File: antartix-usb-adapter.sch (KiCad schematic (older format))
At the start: 113 parts, among them IC1 FT2232D, J1 QTE-020-04-L-D-A, J2 0022232041, J3 614004185023, J4 WE_629105150521, J5 614004185023, J6 614004185023, U1 PCT2075GVX, U2 PAC1934T-I_JQ, U3 USB2514B-I_M2, U4 TPS2024DR, U5 TPS2024DR, U6 TPS2024DR, Y1 7C-24.000MBB-T, Y2 MQ-6.000-12-30_30_

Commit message: Rename alt upstream lanes
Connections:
- net USB_D_CON_N renamed USB_ALT_UP_N
- net USB_D_CON_P renamed USB_ALT_UP_P
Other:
- note added: "Micro USB conn - alternative upstream option"
- note removed: "Micro USB connector"
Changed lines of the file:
@@
 Wire Notes Line
 	4025 525  4025 6650
-Text Notes 12900 3075 0    118  ~ 0
-Micro USB connector
+Text Notes 11650 3075 0    118  ~ 0
+Micro USB conn - alternative upstream option
 Wire Notes Line
 	11575 2850 16075 2850
@@
 $EndComp
 Text Label 575  2225 0    50   ~ 0
-USB_D_CON_N
+USB_ALT_UP_N
 Text Label 575  2125 0    50   ~ 0
-USB_D_CON_P
+USB_ALT_UP_P
 Wire Wire Line
 	1125 2125 550  2125
@@
 $EndComp
 Text Label 13625 3800 2    50   ~ 0
-USB_D_CON_N
+USB_ALT_UP_N
 Text Label 13625 3900 2    50   ~ 0
-USB_D_CON_P
+USB_ALT_UP_P
 Wire Wire Line
 	12625 3900 12900 3900

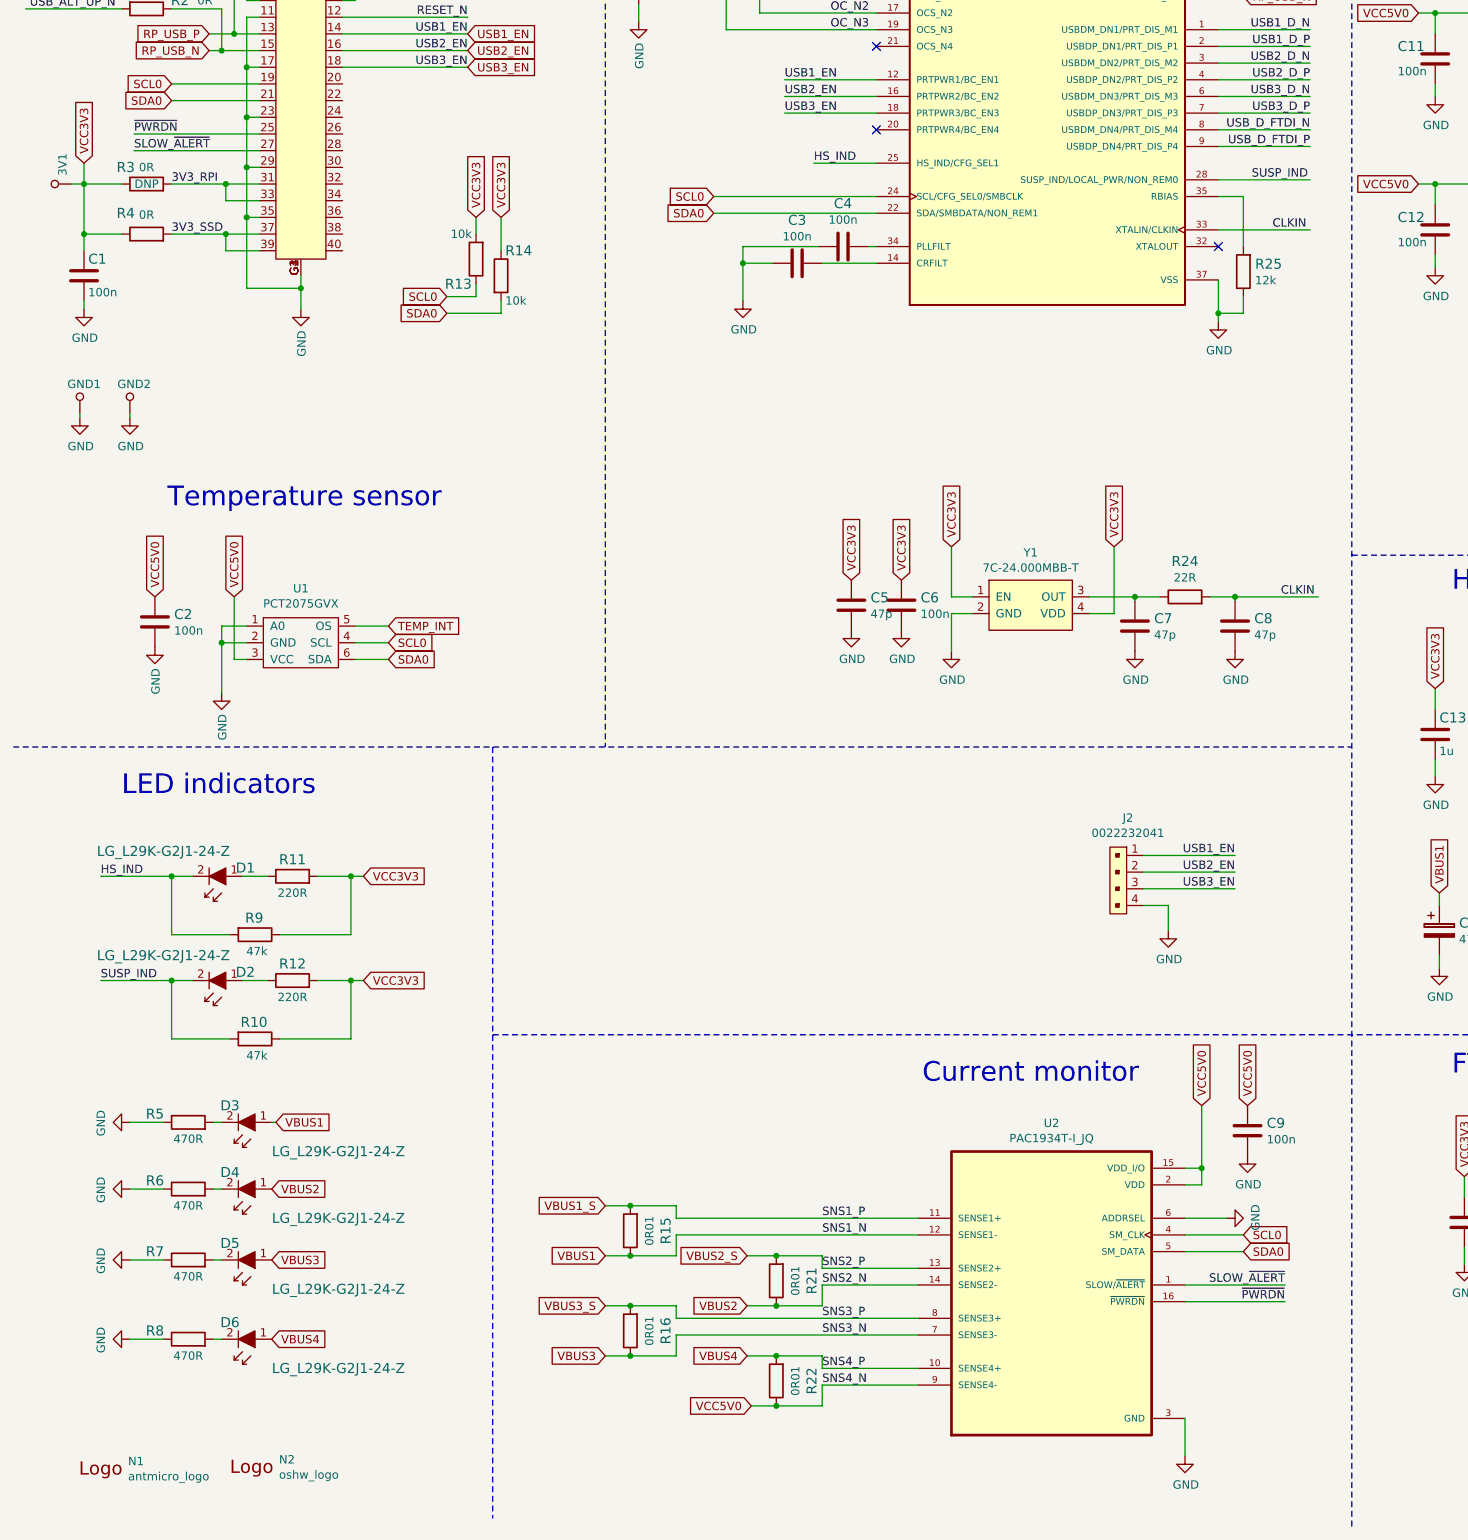
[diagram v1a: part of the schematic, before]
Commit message: Add FTDI and LEDs
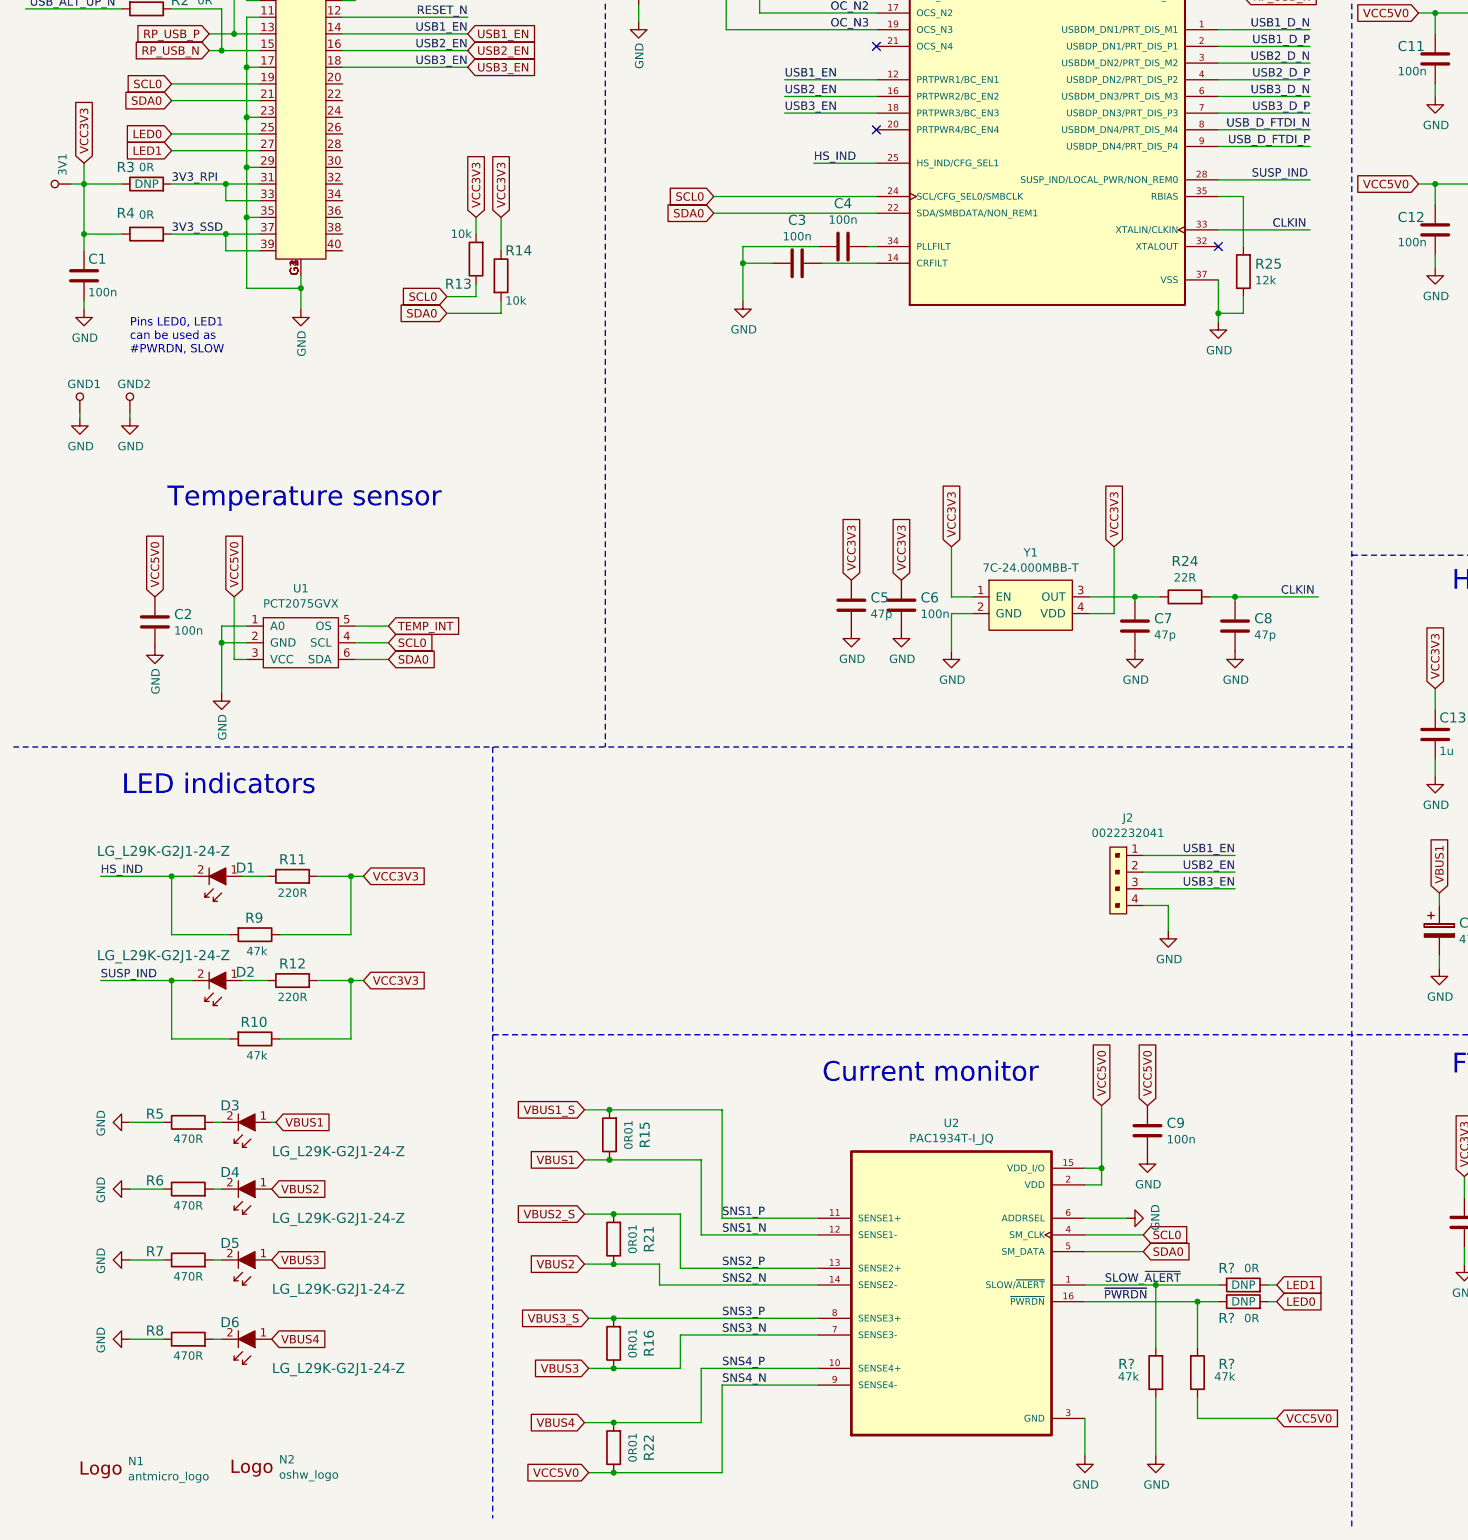
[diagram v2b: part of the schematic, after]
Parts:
- added R? (x2): R_47k_0402, antartix-arty-controller-footprints:0402-res, symbol antartix-arty-controller:R_47k_0402
- added R? (x2): R_0R_0805, antmicro-footprints:0805-res, symbol antmicroResistorsmisc:R_0R_0805
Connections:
- net GND: now also R?.1
- net SLOW_~ALERT: now also R?.1, R?.2; no longer J1.27
- net VCC5V0: now also R?.1
- net ~PWRDN: now also R?.1, R?.2; no longer J1.25
- new net LED0: J1.25, R?.2
- new net LED1: J1.27, R?.2
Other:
- note added: "Pins LED0, LED1\ncan be used as \n#PWRDN, SLOW"
- moved on the sheet: C9, R15, R16, R21, R22, U2

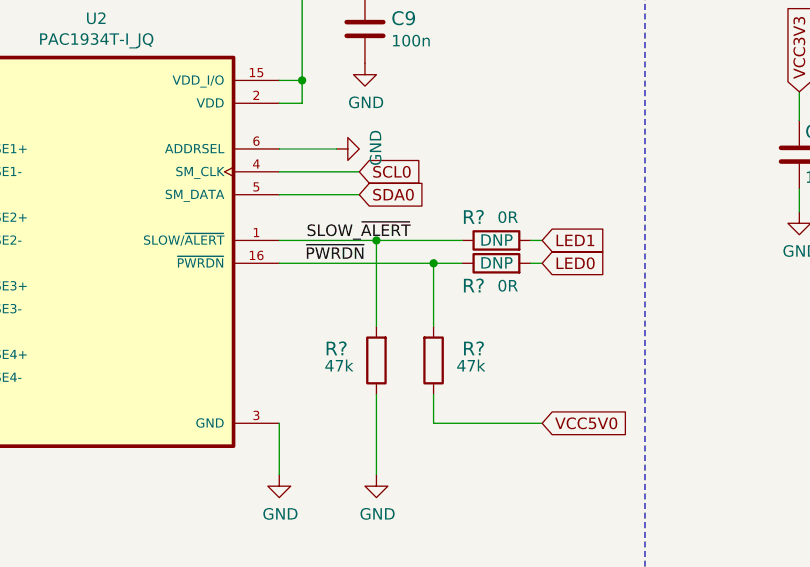
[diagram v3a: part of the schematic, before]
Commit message: Reduce board size, update connector placement
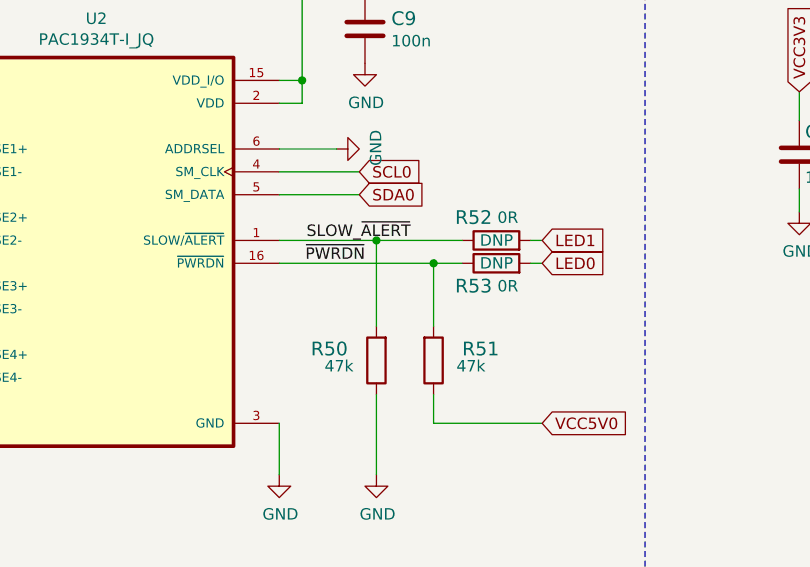
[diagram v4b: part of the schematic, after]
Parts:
- gave numbers to parts that had none: 4
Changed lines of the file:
@@
 P 7325 10400
 AR Path="/60F36AEC" Ref="R?"  Part="1"
-AR Path="/60924187/60F36AEC" Ref="R?"  Part="1"
-F 0 "R?" V 7375 10525 60  0000 L CNN
+AR Path="/60924187/60F36AEC" Ref="R50"  Part="1"
+F 0 "R50" V 7375 10525 60  0000 L CNN
 F 1 "R_47k_0402" H 7325 10250 60  0001 C CNN
 F 2 "antartix-arty-controller-footprints:0402-res" H 7525 10600 60  0001 L CNN
@@
 P 7850 9875
 AR Path="/60F3CD7D" Ref="R?"  Part="1"
-AR Path="/60924187/60F3CD7D" Ref="R?"  Part="1"
-F 0 "R?" H 7750 9975 60  0000 C CNN
+AR Path="/60924187/60F3CD7D" Ref="R52"  Part="1"
+F 0 "R52" H 7750 9975 60  0000 C CNN
 F 1 "R_0R_0805" H 7850 9725 60  0001 C CNN
 F 2 "antmicro-footprints:0805-res" H 8050 10075 60  0001 L CNN
@@
 P 7850 9975
 AR Path="/60F4C618" Ref="R?"  Part="1"
-AR Path="/60924187/60F4C618" Ref="R?"  Part="1"
-F 0 "R?" H 7750 9875 60  0000 C CNN
+AR Path="/60924187/60F4C618" Ref="R53"  Part="1"
+F 0 "R53" H 7750 9875 60  0000 C CNN
 F 1 "R_0R_0805" H 7850 9825 60  0001 C CNN
 F 2 "antmicro-footprints:0805-res" H 8050 10175 60  0001 L CNN
@@
 P 7575 10400
 AR Path="/610F9DE3" Ref="R?"  Part="1"
-AR Path="/60924187/610F9DE3" Ref="R?"  Part="1"
-F 0 "R?" V 7625 10525 60  0000 L CNN
+AR Path="/60924187/610F9DE3" Ref="R51"  Part="1"
+F 0 "R51" V 7625 10525 60  0000 L CNN
 F 1 "R_47k_0402" H 7575 10250 60  0001 C CNN
 F 2 "antartix-arty-controller-footprints:0402-res" H 7775 10600 60  0001 L CNN
@@
 P 7325 10900
 AR Path="/6113774D" Ref="#PWR?"  Part="1"
-AR Path="/60924187/6113774D" Ref="#PWR?"  Part="1"
-F 0 "#PWR?" H 7325 10650 50  0001 C CNN
+AR Path="/60924187/6113774D" Ref="#PWR0119"  Part="1"
+F 0 "#PWR0119" H 7325 10650 50  0001 C CNN
 F 1 "GND" H 7330 10727 50  0000 C CNN
 F 2 "" H 7325 10900 50  0001 C CNN

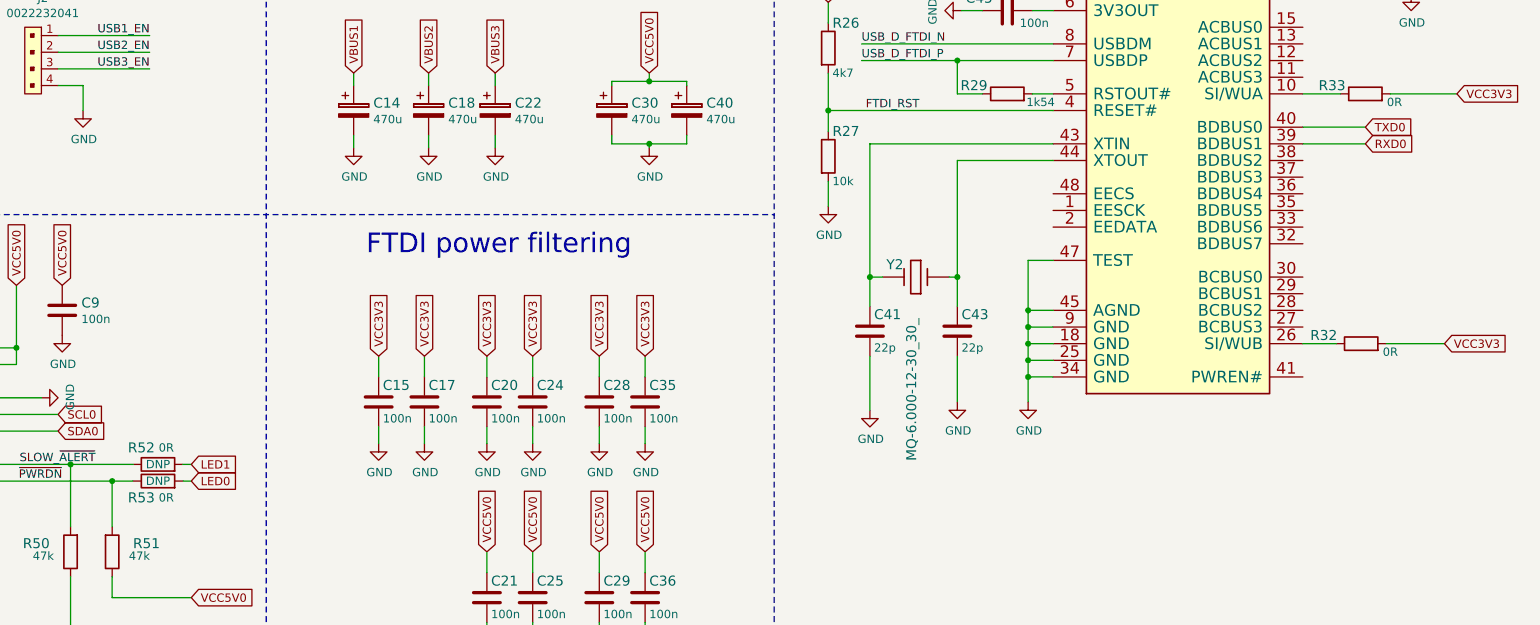
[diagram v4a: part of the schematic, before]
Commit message: Route buttons and HDMI
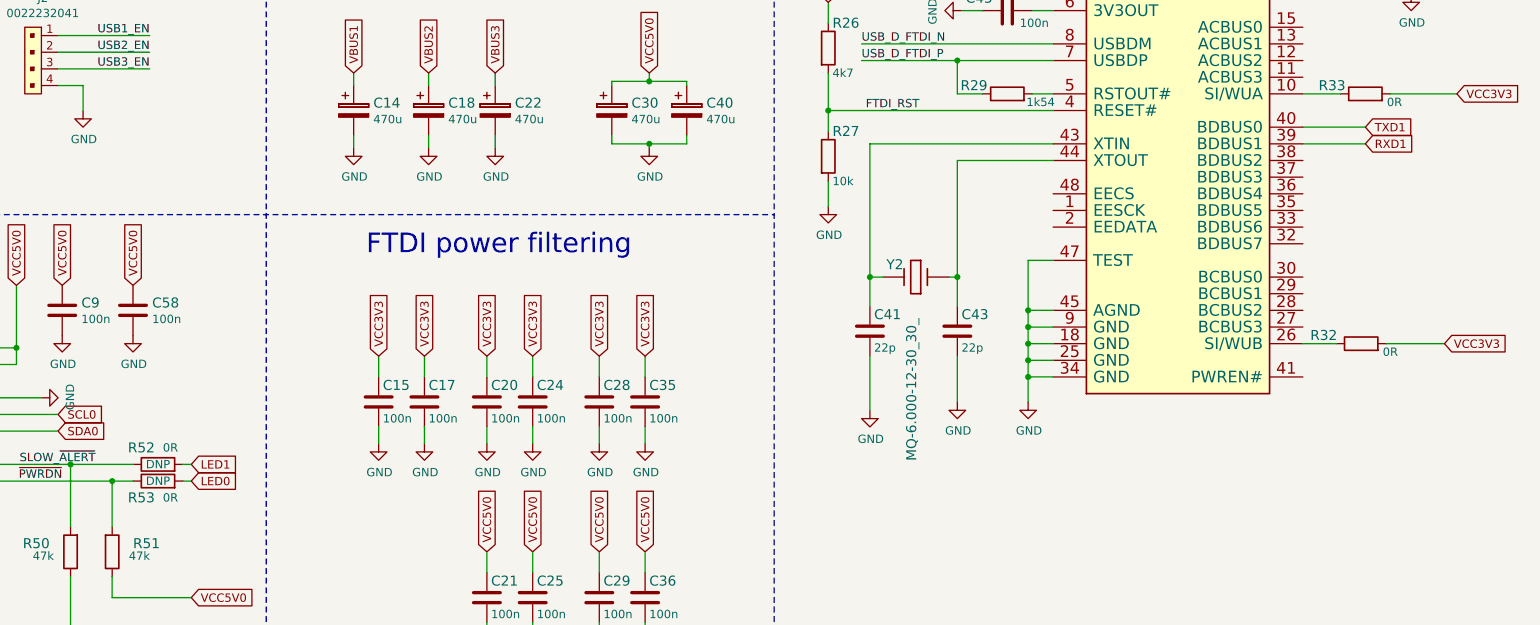
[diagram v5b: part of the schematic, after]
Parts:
- removed R52, R53: R_0R_0805, antmicro-footprints:0805-res, symbol antmicroResistorsmisc:R_0R_0805
- added C58: C_100n_0402, antartix-arty-controller-footprints:0402-cap, symbol antartix-arty-controller:C_100n_0402
- added R52, R53: R_0R_0402, antartix-arty-controller-footprints:0402-res, symbol antartix-arty-controller:R_0R_0402
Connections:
- net GND: now also C58.2
- net LED0: now also R53.2
- net LED1: now also R52.2
- net SLOW_~ALERT: now also R52.1
- net VCC5V0: now also C58.1
- net ~PWRDN: now also R53.1
- net RXD0 renamed RXD1
- net TXD0 renamed TXD1
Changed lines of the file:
@@
 $EndComp
 Text GLabel 15100 7850 2    50   Input ~ 0
-TXD0
+TXD1
 Text GLabel 15100 7950 2    50   Input ~ 0
-RXD0
+RXD1
 Wire Wire Line
 	15100 7850 14725 7850
@@
 	0    -1   -1   0
 $EndComp
-$Comp
-L antmicroResistorsmisc:R_0R_0805 R?
-U 1 1 60F3CD7D
-P 7850 9875
-AR Path="/60F3CD7D" Ref="R?"  Part="1"
-AR Path="/60924187/60F3CD7D" Ref="R52"  Part="1"
-F 0 "R52" H 7750 9975 60  0000 C CNN
-F 1 "R_0R_0805" H 7850 9725 60  0001 C CNN
-F 2 "antmicro-footprints:0805-res" H 8050 10075 60  0001 L CNN
-F 3 "" H 7850 9875 50  0001 C CNN
-F 4 "VISHAY" H 8050 10275 60  0001 L CNN "Manufacturer"
-F 5 "CRCW08050000Z0EA" H 8050 10175 60  0001 L CNN "MPN"
-F 6 "0R" H 7900 9975 50  0000 C CNN "Val"
-F 7 "DNP" H 7850 9875 50  0000 C CNN "Populate"
-	1    7850 9875
-	1    0    0    -1
-$EndComp
-$Comp
-L antmicroResistorsmisc:R_0R_0805 R?
-U 1 1 60F4C618
-P 7850 9975
-AR Path="/60F4C618" Ref="R?"  Part="1"
-AR Path="/60924187/60F4C618" Ref="R53"  Part="1"
-F 0 "R53" H 7750 9875 60  0000 C CNN
-F 1 "R_0R_0805" H 7850 9825 60  0001 C CNN
-F 2 "antmicro-footprints:0805-res" H 8050 10175 60  0001 L CNN
-F 3 "" H 7850 9975 50  0001 C CNN
-F 4 "VISHAY" H 8050 10375 60  0001 L CNN "Manufacturer"
-F 5 "CRCW08050000Z0EA" H 8050 10275 60  0001 L CNN "MPN"
-F 6 "0R" H 7900 9875 50  0000 C CNN "Val"
-F 7 "DNP" H 7850 9975 50  0000 C CNN "Populate"
-	1    7850 9975
-	1    0    0    -1
-$EndComp
 Wire Wire Line
 	6900 9975 7575 9975
@@
 Wire Wire Line
 	7575 10675 7575 10550
+$Comp
+L antartix-arty-controller:R_0R_0402 R53
+U 1 1 605F3D48
+P 7850 9975
+F 0 "R53" H 7750 9875 60  0000 C CNN
+F 1 "R_0R_0402" H 7850 9825 60  0001 C CNN
+F 2 "antartix-arty-controller-footprints:0402-res" H 8050 10175 60  0001 L CNN
+F 3 "" H 7850 9975 50  0001 C CNN
+F 4 "PANASONIC" H 8050 10375 60  0001 L CNN "Manufacturer"
+F 5 "ERJ2GE0R00X" H 8050 10275 60  0001 L CNN "MPN"
+F 6 "0R" H 7925 9875 50  0000 C CNN "Val"
+F 7 "DNP" H 7850 9975 50  0000 C CNN "DNP"
+	1    7850 9975
+	1    0    0    -1
+$EndComp
+$Comp
+L antartix-arty-controller:R_0R_0402 R52
+U 1 1 605F4EE6
+P 7850 9875
+F 0 "R52" H 7750 9975 60  0000 C CNN
+F 1 "R_0R_0402" H 7850 9725 60  0001 C CNN
+F 2 "antartix-arty-controller-footprints:0402-res" H 8050 10075 60  0001 L CNN
+F 3 "" H 7850 9875 50  0001 C CNN
+F 4 "PANASONIC" H 8050 10275 60  0001 L CNN "Manufacturer"
+F 5 "ERJ2GE0R00X" H 8050 10175 60  0001 L CNN "MPN"
+F 6 "0R" H 7925 9975 50  0000 C CNN "Val"
+F 7 "DNP" H 7850 9875 50  0000 C CNN "DNP"
+	1    7850 9875
+	1    0    0    -1
+$EndComp
+$Comp
+L antartix-arty-controller:GND #PWR?
+U 1 1 6060A8DF
+P 7700 9100
+AR Path="/6060A8DF" Ref="#PWR?"  Part="1"
+AR Path="/60924187/6060A8DF" Ref="#PWR0120"  Part="1"
+F 0 "#PWR0120" H 7700 8850 50  0001 C CNN
+F 1 "GND" H 7705 8927 50  0000 C CNN
+F 2 "" H 7700 9100 50  0001 C CNN
+F 3 "" H 7700 9100 50  0001 C CNN
+	1    7700 9100
+	1    0    0    -1
+$EndComp
+Text GLabel 7700 8800 1    50   Input ~ 0
+VCC5V0
+$Comp
+L antartix-arty-controller:C_100n_0402 C?
+U 1 1 6060A8E9
+P 7700 8950
+AR Path="/6060A8E9" Ref="C?"  Part="1"
+AR Path="/60924187/6060A8E9" Ref="C58"  Part="1"
+F 0 "C58" H 7815 8995 60  0000 L CNN
+F 1 "C_100n_0402" H 7700 8800 60  0001 C CNN
+F 2 "antartix-arty-controller-footprints:0402-cap" H 7900 9150 60  0001 L CNN
+F 3 "" H 7700 8950 50  0001 C CNN
+F 4 "Walsin" H 7900 9350 60  0001 L CNN "Manufacturer"
+F 5 "0402X104K6R3CT" H 7900 9250 60  0001 L CNN "MPN"
+F 6 "100n" H 7815 8897 50  0000 L CNN "Val"
+	1    7700 8950
+	1    0    0    -1
+$EndComp
 $EndSCHEMATC
